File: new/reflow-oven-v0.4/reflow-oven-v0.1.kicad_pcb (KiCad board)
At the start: 2 copper layers, 67.9 x 100 mm, 7 parts, among them IC1 MBED-LPC1768, J1 Pot, J3 Conn_01x01_Female, J4 Conn_01x01_Female, U1 MOC3041M

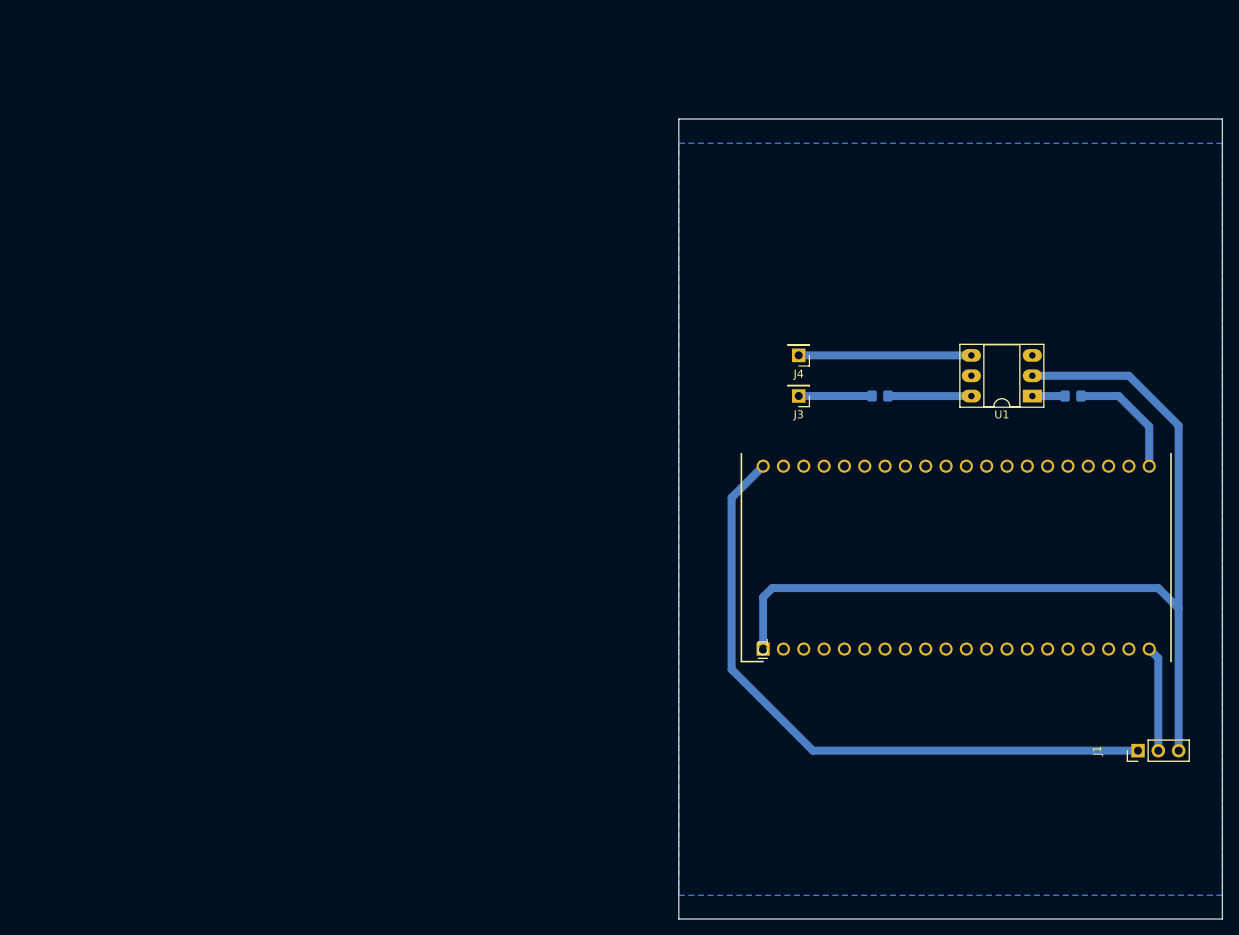
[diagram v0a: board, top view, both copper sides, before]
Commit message: Added PCB schematic for prototyping
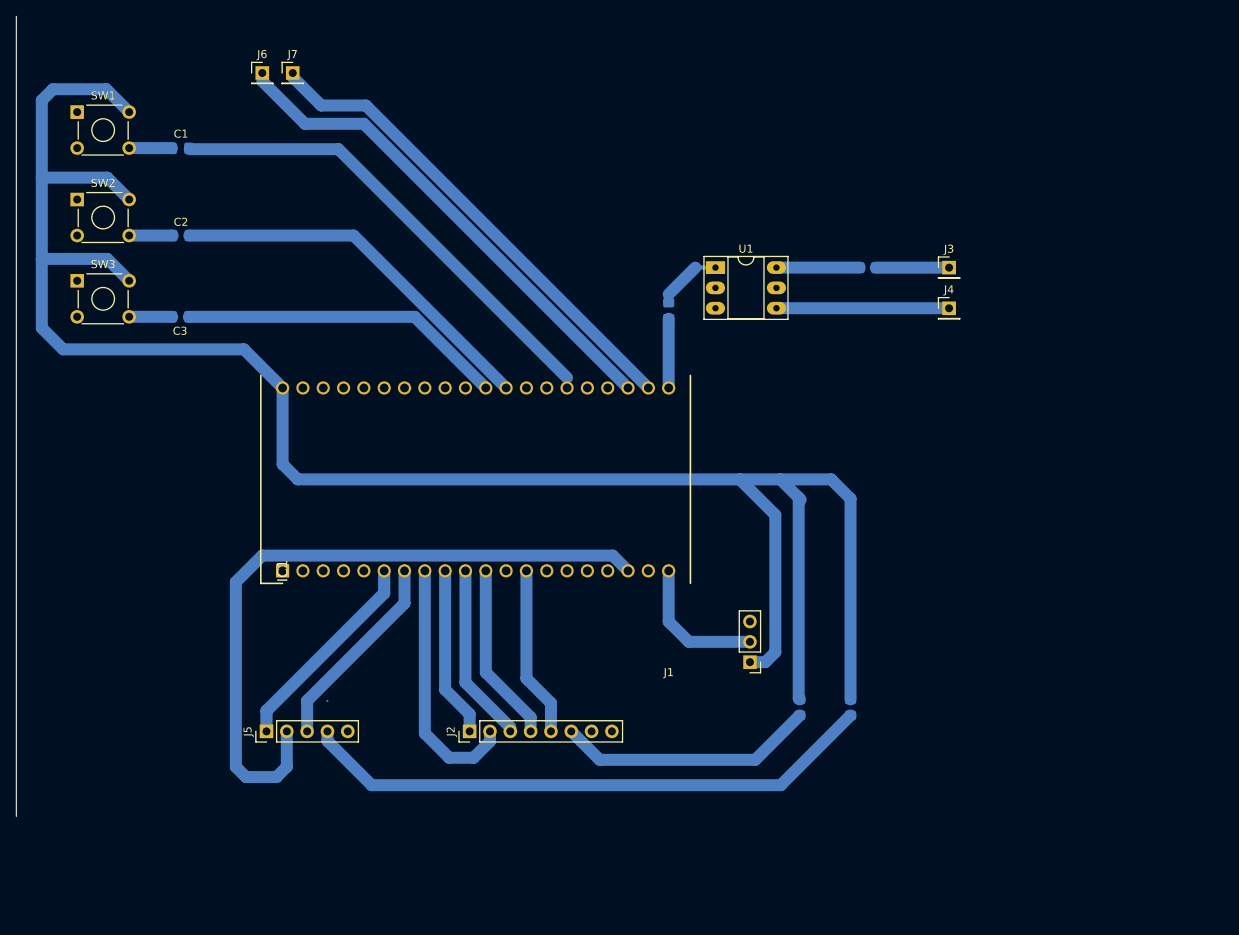
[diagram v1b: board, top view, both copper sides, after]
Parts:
- added C1: 1u, Capacitor_SMD:C_0805_2012Metric_Pad1.18x1.45mm_HandSolder, B.Cu at (71.1, 61.5)
- added C2: 1u, Capacitor_SMD:C_0805_2012Metric_Pad1.18x1.45mm_HandSolder, B.Cu at (71.1, 72.4)
- added C3: 1u, Capacitor_SMD:C_0805_2012Metric_Pad1.18x1.45mm_HandSolder, B.Cu at (71.1, 82.5)
- added J2: Conn_01x08_Female, Connector_PinHeader_2.54mm:PinHeader_1x08_P2.54mm_Vertical, F.Cu at (107.2, 134.4)
- added J5: Conn_01x05_Female, Connector_PinHeader_2.54mm:PinHeader_1x05_P2.54mm_Vertical, F.Cu at (81.8, 134.4)
- added J6: Conn_01x01_Female, Connector_PinHeader_2.54mm:PinHeader_1x01_P2.54mm_Vertical, F.Cu at (81.3, 52.1)
- added J7: Conn_01x01_Female, Connector_PinHeader_2.54mm:PinHeader_1x01_P2.54mm_Vertical, F.Cu at (85.1, 52.1)
- added R3: 560, Resistor_SMD:R_0805_2012Metric_Pad1.20x1.40mm_HandSolder, B.Cu at (148.5, 131.4)
- added R4: 69, Resistor_SMD:R_0805_2012Metric_Pad1.20x1.40mm_HandSolder, B.Cu at (154.8, 131.4)
- added SW1: pb1, Button_Switch_THT:SW_TH_Tactile_Omron_B3F-10xx, F.Cu at (58.1, 57.0)
- added SW2: pb2, Button_Switch_THT:SW_TH_Tactile_Omron_B3F-10xx, F.Cu at (58.1, 67.9)
- added SW3: pb3, Button_Switch_THT:SW_TH_Tactile_Omron_B3F-10xx, F.Cu at (58.1, 78.0)
- moved IC1 60.9 mm to (83.8, 114.3)
- moved R1 51.7 mm to (132.1, 81.8), turned to 90 degrees
- moved J1 49.8 mm to (142.2, 125.7), turned to 180 degrees
- moved U1 42.7 mm to (137.9, 76.4), turned to 0 degrees
- moved J3 24.7 mm to (167.1, 76.4), turned to 0 degrees
- moved J4 19.7 mm to (167.1, 81.5), turned to 0 degrees
- moved R2 16.1 mm to (157.0, 76.4), turned to 0 degrees
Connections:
- net /PWM renamed pwm-psac
- net Net-(J1-Pad2) renamed Analogin-pot
- IC1 pad 10: unconnected-(IC1-Pad10) -> mosi_lcd
- IC1 pad 11: unconnected-(IC1-Pad11) -> mosi_lcd
- IC1 pad 13: unconnected-(IC1-Pad13) -> sck_lcd
- IC1 pad 18: unconnected-(IC1-Pad18) -> chip_select_max
- IC1 pad 22: unconnected-(IC1-Pad22) -> pwm-extra1
- IC1 pad 23: unconnected-(IC1-Pad23) -> pwm-extra2
- IC1 pad 26: unconnected-(IC1-Pad26) -> push-button1
- IC1 pad 29: unconnected-(IC1-Pad29) -> push-button2
- IC1 pad 30: unconnected-(IC1-Pad30) -> push-button3
- IC1 pad 6: unconnected-(IC1-Pad6) -> miso_max
- IC1 pad 7: unconnected-(IC1-Pad7) -> sck_max
- IC1 pad 8: unconnected-(IC1-Pad8) -> chip_select_lcd
- IC1 pad 9: unconnected-(IC1-Pad9) -> rst_lcd
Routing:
- net VCC: track 82.0 -> 262.4 mm
- net GND: track 121.4 -> 0.00 mm
- net chip_select_max: track 0.00 -> 86.1 mm
- net Net-(J5-Pad4): track 0.00 -> 72.5 mm
- net pwm-extra2: track 0.00 -> 62.6 mm
- net pwm-extra1: track 0.00 -> 61.1 mm
- net push-button1: track 0.00 -> 60.6 mm
- net push-button2: track 0.00 -> 47.5 mm
- net mosi_lcd: track 0.00 -> 44.8 mm
- net push-button3: track 0.00 -> 40.8 mm
- net Net-(J2-Pad6): track 0.00 -> 32.5 mm
- net chip_select_lcd: track 0.00 -> 31.8 mm
- net miso_max: track 0.00 -> 26.2 mm
- net sck_max: track 0.00 -> 25.1 mm
- net rst_lcd: track 0.00 -> 21.5 mm
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- removed copper zone on B.Cu, net GND
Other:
- board outline removed

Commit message: Update schematic
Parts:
- SW1, SW2, SW3: footprint Button_Switch_THT:SW_TH_Tactile_Omron_B3F-10xx -> Button_Switch_THT:SW_Tactile_SKHH_Angled
- moved J3 44.1 mm to (128.8, 54.6)
- moved J4 44.1 mm to (128.8, 59.7)
- moved R2 42.4 mm to (120.7, 54.6)
- moved R4 29.9 mm to (125.1, 128.2)
- moved R3 28.2 mm to (120.4, 128.3)
- moved J1 27.1 mm to (115.8, 119.7), turned to 0 degrees
- moved U1 21.7 mm to (116.3, 74.7), turned to 90 degrees
- moved IC1 20.4 mm to (64.0, 109.5)
- moved J2 18.8 mm to (88.4, 133.1)
- moved J5 18.8 mm to (63.0, 133.1)
- moved R1 15.9 mm to (116.3, 79.8)
- moved C1 9.50 mm to (64.3, 54.9)
- moved C2 8.99 mm to (64.5, 66.3)
- moved C3 8.14 mm to (64.5, 77.7)
- moved SW3 4.20 mm to (54.4, 80.0), turned to 90 degrees
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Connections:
- IC1 pad 10: mosi_lcd -> data_command_lcd
- J2 pad 3: mosi_lcd -> data_command_lcd
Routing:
- net GND: track 0.00 -> 95.8 mm, vias 0 -> 3
- net VCC: track 262.4 -> 189.9 mm
- net data_command_lcd: track 0.00 -> 26.4 mm
- net mosi_lcd: track 44.8 -> 26.4 mm
- net pwm-extra2: track 62.6 -> 45.3 mm
- net pwm-extra1: track 61.1 -> 44.8 mm
- net push-button3: track 40.8 -> 30.6 mm
- net push-button1: track 60.6 -> 50.5 mm
- net Net-(J5-Pad4): track 72.5 -> 62.4 mm
- net push-button2: track 47.5 -> 38.0 mm
- net Net-(J4-Pad1): track 21.6 -> 12.8 mm
- net Net-(J2-Pad6): track 32.5 -> 23.8 mm
- net chip_select_max: track 86.1 -> 93.3 mm
- net chip_select_lcd: track 31.8 -> 36.8 mm
- net Net-(C3-Pad2): track 5.39 -> 9.97 mm
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- added copper zone on B.Cu, net (none)
- added copper zone on B.Cu, net GND
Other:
- board outline added: 125.2 x 100 mm
